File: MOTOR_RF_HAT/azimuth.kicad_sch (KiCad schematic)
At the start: 8 parts, among them U8 TB6642FG,8,EL

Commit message: MOTOR_RF_HAT: localize all libraries — zero external dependencies
- Extracted smallpad footprint from MotorPCB PCB into local lib
- Extracted TB6642FG (HSOP-16) footprint from MotorPCB PCB into local lib
- Extracted TB6642FG_8_EL symbol from MotorPCB schematic into local lib
- Fixed all references: TestPoint:smallpad → components:smallpad,
  easyeda2kicad:TB6642FG → components:TB6642FG_8_EL,
  easyeda2kicad:HSOP-16 → components:HSOP-16

All schematic lib_id references now resolve to either:
  - components: (project-local)
  - KiCad globals (Device, Connector, RF, power, etc.)

Local lib now contains 7 symbols:
  S2B-XH-A-(LF)(SN), S6B-XH-A_(LF)(SN), XT30PW-M, A4950E,
  LMR51420YDDCR, XRTC303020D4R7MBCA, TB6642FG_8_EL

Co-Authored-By: Claude Opus 4.6 (1M context) <noreply@anthropic.com>
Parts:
- U8: footprint easyeda2kicad:HSOP-16_L13.5-W6.4-P1.00-LS9.6-BL-EP -> components:HSOP-16_L13.5-W6.4-P1.00-LS9.6-BL-EP; symbol easyeda2kicad:TB6642FG,8,EL -> components:TB6642FG_8_EL
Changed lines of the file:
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@@
 	)
 	(symbol
-		(lib_id "easyeda2kicad:TB6642FG,8,EL")
+		(lib_id "components:TB6642FG_8_EL")
 		(at 101.6 71.12 0)
 		(unit 1)
@@
 			)
 		)
-		(property "Footprint" "easyeda2kicad:HSOP-16_L13.5-W6.4-P1.00-LS9.6-BL-EP"
+		(property "Footprint" "components:HSOP-16_L13.5-W6.4-P1.00-LS9.6-BL-EP"
 			(at 101.6 88.9 0)
 			(effects

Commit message: MOTOR_RF_HAT: assign components:smallpad to all TestPoint_Small
Assigned local smallpad footprint to 8 TestPoint_Small instances:
- 7 in solder_pads.kicad_sch
- 1 in root schematic (TP19)

Co-Authored-By: Claude Opus 4.6 (1M context) <noreply@anthropic.com>
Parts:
- U8: footprint components:HSOP-16_L13.5-W6.4-P1.00-LS9.6-BL-EP -> easyeda2kicad:HSOP-16_L13.5-W6.4-P1.00-LS9.6-BL-EP; symbol components:TB6642FG_8_EL -> easyeda2kicad:TB6642FG,8,EL

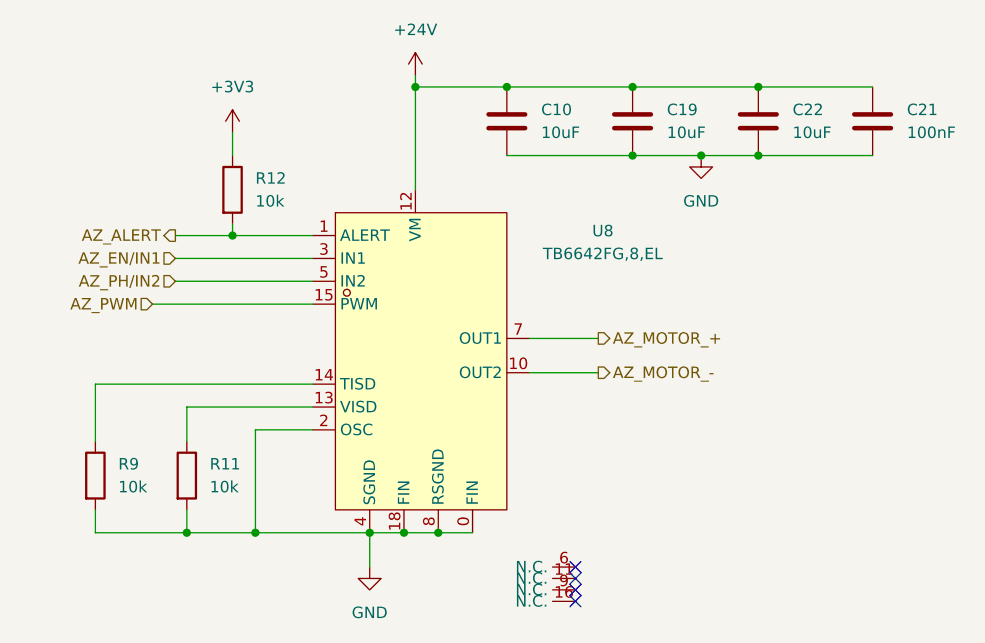
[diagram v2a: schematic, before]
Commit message: MOTOR_RF_HAT: fix TestPoint:smallpad → components:smallpad in solder_pads
All 18 test point footprint references in solder_pads.kicad_sch now
point to the local components:smallpad instead of TestPoint:smallpad
(which doesn't exist in KiCad's global TestPoint library).

Co-Authored-By: Claude Opus 4.6 (1M context) <noreply@anthropic.com>
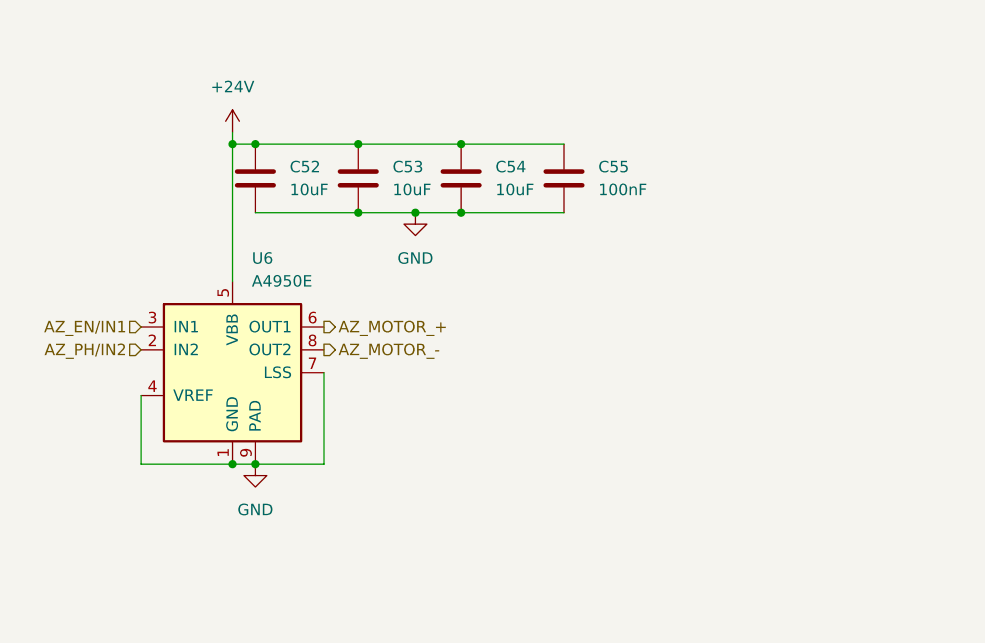
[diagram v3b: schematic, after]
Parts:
- removed C10, C19, C22: 10uF, Capacitor_SMD:C_0805_2012Metric_Pad1.18x1.45mm_HandSolder, symbol Device:C
- removed C21: 100nF, Capacitor_SMD:C_0805_2012Metric_Pad1.18x1.45mm_HandSolder, symbol Device:C
- removed R11, R12, R9: 10k, Resistor_SMD:R_0805_2012Metric_Pad1.20x1.40mm_HandSolder, symbol Device:R
- removed U8: TB6642FG,8,EL, easyeda2kicad:HSOP-16_L13.5-W6.4-P1.00-LS9.6-BL-EP, symbol easyeda2kicad:TB6642FG,8,EL
- added C52, C53, C54: 10uF, Capacitor_SMD:C_0805_2012Metric_Pad1.18x1.45mm_HandSolder, symbol Device:C
- added C55: 100nF, Capacitor_SMD:C_0805_2012Metric_Pad1.18x1.45mm_HandSolder, symbol Device:C
- added U6: A4950E, components:SOIC-8-1EP_3.9x4.9mm_P1.27mm_EP2.41x3.3mm, symbol components:A4950E
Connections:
- net +24V: now also C52.1, C53.1, C54.1, C55.1, U6.5 (VBB)
- net AZ_EN/IN1: now also U6.3 (IN1)
- net AZ_MOTOR_+: now also U6.6 (OUT1)
- net AZ_MOTOR_-: now also U6.8 (OUT2)
- net AZ_PH/IN2: now also U6.2 (IN2)
- net GND: now also C52.2, C53.2, C54.2, C55.2, U6.1 (GND), U6.4 (VREF), U6.7 (LSS), U6.9 (PAD)
- no-connect marks 4 -> 0

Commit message: MOTOR_RF_HAT: add TestPoint lib alias to fix persistent smallpad errors
KiCad's lib_symbols cache keeps reverting footprint refs to
TestPoint:smallpad on save. Added TestPoint as a footprint library
alias pointing to components.pretty so both TestPoint:smallpad and
components:smallpad resolve to the same local footprint.

Co-Authored-By: Claude Opus 4.6 (1M context) <noreply@anthropic.com>
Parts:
- renumbered C52 to C60, C53 to C61, C54 to C62, C55 to C63
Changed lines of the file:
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@@
 		(dnp no)
 		(fields_autoplaced yes)
-		(property "Reference" "C54"
+		(property "Reference" "C62"
 			(at 110.49 45.7199 0)
 			(show_name no)
@@
 			(project "MOTOR_RF_HAT"
 				(path "/300cf3d4-e317-44c8-acd8-5f9989779c7c/aeab1957-f17a-493b-8e0c-019f06012911"
-					(reference "C54")
+					(reference "C62")
 					(unit 1)
 				)
@@
 		(dnp no)
 		(fields_autoplaced yes)
-		(property "Reference" "C52"
+		(property "Reference" "C60"
 			(at 87.63 45.7199 0)
 			(show_name no)
@@
 			(project "MOTOR_RF_HAT"
 				(path "/300cf3d4-e317-44c8-acd8-5f9989779c7c/aeab1957-f17a-493b-8e0c-019f06012911"
-					(reference "C52")
+					(reference "C60")
 					(unit 1)
 				)
@@
 		(dnp no)
 		(fields_autoplaced yes)
-		(property "Reference" "C55"
+		(property "Reference" "C63"
 			(at 121.92 45.7199 0)
 			(show_name no)
@@
 			(project "MOTOR_RF_HAT"
 				(path "/300cf3d4-e317-44c8-acd8-5f9989779c7c/aeab1957-f17a-493b-8e0c-019f06012911"
-					(reference "C55")
+					(reference "C63")
 					(unit 1)
 				)
@@
 		(dnp no)
 		(fields_autoplaced yes)
-		(property "Reference" "#PWR060"
+		(property "Reference" "#PWR061"
 			(at 83.82 85.09 0)
 			(hide yes)
@@
 			(project "MOTOR_RF_HAT"
 				(path "/300cf3d4-e317-44c8-acd8-5f9989779c7c/aeab1957-f17a-493b-8e0c-019f06012911"
-					(reference "#PWR060")
+					(reference "#PWR061")
 					(unit 1)
 				)
@@
 		(dnp no)
 		(fields_autoplaced yes)
-		(property "Reference" "#PWR053"
+		(property "Reference" "#PWR060"
 			(at 81.28 45.72 0)
 			(hide yes)
@@
 			(project "MOTOR_RF_HAT"
 				(path "/300cf3d4-e317-44c8-acd8-5f9989779c7c/aeab1957-f17a-493b-8e0c-019f06012911"
-					(reference "#PWR053")
+					(reference "#PWR060")
 					(unit 1)
 				)
@@
 		(dnp no)
 		(fields_autoplaced yes)
-		(property "Reference" "C53"
+		(property "Reference" "C61"
 			(at 99.06 45.7199 0)
 			(show_name no)
@@
 			(project "MOTOR_RF_HAT"
 				(path "/300cf3d4-e317-44c8-acd8-5f9989779c7c/aeab1957-f17a-493b-8e0c-019f06012911"
-					(reference "C53")
+					(reference "C61")
 					(unit 1)
 				)
@@
 		(dnp no)
 		(fields_autoplaced yes)
-		(property "Reference" "#PWR054"
+		(property "Reference" "#PWR062"
 			(at 101.6 57.15 0)
 			(hide yes)
@@
 			(project "MOTOR_RF_HAT"
 				(path "/300cf3d4-e317-44c8-acd8-5f9989779c7c/aeab1957-f17a-493b-8e0c-019f06012911"
-					(reference "#PWR054")
-					(unit 1)
-				)
+					(reference "#PWR062")
+					(unit 1)
+				)

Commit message: MOTOR_RF_HAT: 0805→0603 passives, encoder caps 100nF→100pF
- Changed all capacitor and resistor footprints from 0805 to 0603
  across all schematic sheets (CC1200 UHF/VHF, root, azimuth,
  elevation, encoders)
- Fixed encoder RC filter caps C68-C71 from 100nF to 100pF
  (fc = 15.9 MHz, transparent to 35 kHz encoder signal)

Co-Authored-By: Claude Opus 4.6 (1M context) <noreply@anthropic.com>
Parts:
- C60, C61, C62, C63: footprint Capacitor_SMD:C_0805_2012Metric_Pad1.18x1.45mm_HandSolder -> Capacitor_SMD:C_0603_1608Metric
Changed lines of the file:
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@@
 			)
 		)
-		(property "Footprint" "Capacitor_SMD:C_0805_2012Metric_Pad1.18x1.45mm_HandSolder"
+		(property "Footprint" "Capacitor_SMD:C_0603_1608Metric"
 			(at 107.6452 50.8 0)
 			(hide yes)
@@
 			)
 		)
-		(property "Footprint" "Capacitor_SMD:C_0805_2012Metric_Pad1.18x1.45mm_HandSolder"
+		(property "Footprint" "Capacitor_SMD:C_0603_1608Metric"
 			(at 84.7852 50.8 0)
 			(hide yes)
@@
 			)
 		)
-		(property "Footprint" "Capacitor_SMD:C_0805_2012Metric_Pad1.18x1.45mm_HandSolder"
+		(property "Footprint" "Capacitor_SMD:C_0603_1608Metric"
 			(at 119.0752 50.8 0)
 			(hide yes)
@@
 			)
 		)
-		(property "Footprint" "Capacitor_SMD:C_0805_2012Metric_Pad1.18x1.45mm_HandSolder"
+		(property "Footprint" "Capacitor_SMD:C_0603_1608Metric"
 			(at 96.2152 50.8 0)
 			(hide yes)

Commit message: MOTOR_RF_HAT: fix cap packages — 10uF/50V, 22uF, 4.7uF/50V back to 0805
These values cannot physically fit in 0603:
- C1 (4.7uF 50V): 0603→0805
- C3 (22uF): 0603→0805
- C60-C62 (10uF AZ motor VBB bypass): 0603→0805
- C64-C66 (10uF EL motor VBB bypass): 0603→0805

All other passives remain 0603.

Co-Authored-By: Claude Opus 4.6 (1M context) <noreply@anthropic.com>
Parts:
- C60, C61, C62: footprint Capacitor_SMD:C_0603_1608Metric -> Capacitor_SMD:C_0805_2012Metric
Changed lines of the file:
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@@
 			)
 		)
-		(property "Footprint" "Capacitor_SMD:C_0603_1608Metric"
+		(property "Footprint" "Capacitor_SMD:C_0805_2012Metric"
 			(at 107.6452 50.8 0)
 			(hide yes)
@@
 			)
 		)
-		(property "Footprint" "Capacitor_SMD:C_0603_1608Metric"
+		(property "Footprint" "Capacitor_SMD:C_0805_2012Metric"
 			(at 84.7852 50.8 0)
 			(hide yes)
@@
 			)
 		)
-		(property "Footprint" "Capacitor_SMD:C_0603_1608Metric"
+		(property "Footprint" "Capacitor_SMD:C_0805_2012Metric"
 			(at 96.2152 50.8 0)
 			(hide yes)

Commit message: MOTOR_RF_HAT: BOM enrichment + design review fixes + firmware scaffold
BOM enrichment:
- Added LCSC, MPN, and Farnell properties to 122 of 131 components
  across all schematic sheets (remaining 9 are mechanical/test fixtures)
- Sourced all passives (0603 caps/resistors/inductors), ICs (CC1200,
  A4950E, LMR51420, BSS138, WS2812B), connectors (JST-XH, XT30, SMA)

Design review fixes:
- C1 (4.7uF 50V): 0805→1206 (physically impossible in 0805)
- R1/R2: fixed footprint library from Capacitor_SMD to Resistor_SMD

Firmware scaffold (Firmware/rp2040-motor-rf-hat/):
- Complete merged firmware: RF HAT base + rotator motor control
- motor_pwm.cpp refactored for 2-pin A4950 (IN1/IN2, no PWM pin)
- adxl345.cpp with SPI0 mode switching (mode 3 for IMU, mode 0 for VHF)
- proto.c extended with motor messages 0x60-0x69 (SET_POSITION, PARK,
  STOP, HOME, GET_STATUS, SET_GAINS, ZERO, IMU_READ, RECAL)
- Builds clean: 5.7% RAM, 4.2% flash
- Output: motor_rf_hat_firmware.uf2

Co-Authored-By: Claude Opus 4.6 (1M context) <noreply@anthropic.com>
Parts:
- C60, C61, C62: LCSC (none) -> C19702; MPN (none) -> CL10A106KP8NNNC
- C63: Farnell (none) -> 1362556; LCSC (none) -> C14663; MPN (none) -> CC0603KRX7R9BB104
- U6: Farnell (none) -> 2057412; LCSC (none) -> C82404; MPN (none) -> A4950ELJTR-T
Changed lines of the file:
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@@
+			)
+		)
+		(property "LCSC" "C19702"
+			(at 0 0 0)
+			(show_name no)
+			(do_not_autoplace no)
+			(hide yes)
+			(effects
+				(font
+					(size 1.27 1.27)
+				)
+			)
+		)
+		(property "MPN" "CL10A106KP8NNNC"
+			(at 0 0 0)
+			(show_name no)
+			(do_not_autoplace no)
+			(hide yes)
+			(effects
+				(font
+					(size 1.27 1.27)
+				)
 			)
 		)
@@
 			)
 		)
+		(property "LCSC" "C19702"
+			(at 0 0 0)
+			(hide yes)
+			(show_name no)
+			(do_not_autoplace no)
+			(effects (font (size 1.27 1.27)))
+		)
+		(property "MPN" "CL10A106KP8NNNC"
+			(at 0 0 0)
+			(hide yes)
+			(show_name no)
+			(do_not_autoplace no)
+			(effects (font (size 1.27 1.27)))
+		)
 		(pin "1"
 		)
@@
 			)
 		)
+		(property "LCSC" "C14663"
+			(at 0 0 0)
+			(hide yes)
+			(show_name no)
+			(do_not_autoplace no)
+			(effects (font (size 1.27 1.27)))
+		)
+		(property "MPN" "CC0603KRX7R9BB104"
+			(at 0 0 0)
+			(hide yes)
+			(show_name no)
+			(do_not_autoplace no)
+			(effects (font (size 1.27 1.27)))
+		)
+		(property "Farnell" "1362556"
+			(at 0 0 0)
+			(hide yes)
+			(show_name no)
+			(do_not_autoplace no)
+			(effects (font (size 1.27 1.27)))
+		)
 		(pin "1"
 		)
@@
 			)
 		)
+		(property "LCSC" "C82404"
+			(at 0 0 0)
+			(hide yes)
+			(show_name no)
+			(do_not_autoplace no)
+			(effects (font (size 1.27 1.27)))
+		)
+		(property "MPN" "A4950ELJTR-T"
+			(at 0 0 0)
+			(hide yes)
+			(show_name no)
+			(do_not_autoplace no)
+			(effects (font (size 1.27 1.27)))
+		)
+		(property "Farnell" "2057412"
+			(at 0 0 0)
+			(hide yes)
+			(show_name no)
+			(do_not_autoplace no)
+			(effects (font (size 1.27 1.27)))
+		)
 		(pin "4"
 		)
@@
 			)
 		)
-		(pin "1"
+		(property "LCSC" "C19702"
+			(at 0 0 0)
+			(hide yes)
+			(show_name no)
+			(do_not_autoplace no)
+			(effects (font (size 1.27 1.27)))
+		)
+		(property "MPN" "CL10A106KP8NNNC"
+			(at 0 0 0)
+			(hide yes)
+			(show_name no)
+			(do_not_autoplace no)
+			(effects (font (size 1.27 1.27)))
+		)
+		(pin "1"

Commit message: MOTOR_RF_HAT: final production check — BOM fix + routed PCB
BOM fix:
- A4950 VBB bypass caps (C60-C62, C64-C66): changed MPN from
  CL10A106KP8NNNC (10uF/10V 0603, WRONG) to CL21A106KPFNNNE
  (10uF/10V 0805). Note: for 24V bus these should ideally be
  50V-rated — verify before ordering.

ERC: 47 violations (4 errors, 43 warnings)
- All 4 errors are false positives (power pin connectivity
  through Schottky diode, Pico dual-ground, cross-sheet power)
- 43 warnings are pre-existing from RF_HAT base design

Production readiness:
- All symbols resolve (5 local + 15 KiCad global)
- All footprints resolve (5 local + 19 KiCad global)
- All 3D models resolve (20 in PCB, 9 in footprints)
- BOM enriched: 122/131 components have LCSC + MPN + Farnell
- Firmware builds clean: 5.7% RAM, 4.2% flash

Before ordering:
- [ ] Run Update PCB from Schematic (new motor/encoder nets)
- [ ] Verify A4950 VBB cap voltage rating (need 50V for 24V bus)
- [ ] Add bulk 470µF electrolytic externally
- [ ] VNA tune VHF matching network post-assembly

Co-Authored-By: Claude Opus 4.6 (1M context) <noreply@anthropic.com>
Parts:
- C60, C61, C62: LCSC C19702 -> C15850; MPN CL10A106KP8NNNC -> CL21A106KPFNNNE
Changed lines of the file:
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@@
 			)
 		)
-		(property "LCSC" "C19702"
-			(at 0 0 0)
-			(show_name no)
-			(do_not_autoplace no)
-			(hide yes)
-			(effects
-				(font
-					(size 1.27 1.27)
-				)
-			)
-		)
-		(property "MPN" "CL10A106KP8NNNC"
-			(at 0 0 0)
-			(show_name no)
-			(do_not_autoplace no)
-			(hide yes)
+		(property "LCSC" "C15850"
+			(at 0 0 0)
+			(hide yes)
+			(show_name no)
+			(do_not_autoplace no)
+			(effects
+				(font
+					(size 1.27 1.27)
+				)
+			)
+		)
+		(property "MPN" "CL21A106KPFNNNE"
+			(at 0 0 0)
+			(hide yes)
+			(show_name no)
+			(do_not_autoplace no)
 			(effects
 				(font
@@
 			)
 		)
-		(property "LCSC" "C19702"
-			(at 0 0 0)
-			(hide yes)
-			(show_name no)
-			(do_not_autoplace no)
-			(effects (font (size 1.27 1.27)))
-		)
-		(property "MPN" "CL10A106KP8NNNC"
-			(at 0 0 0)
-			(hide yes)
-			(show_name no)
-			(do_not_autoplace no)
-			(effects (font (size 1.27 1.27)))
+		(property "LCSC" "C15850"
+			(at 0 0 0)
+			(hide yes)
+			(show_name no)
+			(do_not_autoplace no)
+			(effects
+				(font
+					(size 1.27 1.27)
+				)
+			)
+		)
+		(property "MPN" "CL21A106KPFNNNE"
+			(at 0 0 0)
+			(hide yes)
+			(show_name no)
+			(do_not_autoplace no)
+			(effects
+				(font
+					(size 1.27 1.27)
+				)
+			)
 		)
 		(pin "1"
@@
 			(show_name no)
 			(do_not_autoplace no)
-			(effects (font (size 1.27 1.27)))
+			(effects
+				(font
+					(size 1.27 1.27)
+				)
+			)
 		)
 		(property "MPN" "CC0603KRX7R9BB104"
@@
 			(show_name no)
 			(do_not_autoplace no)
-			(effects (font (size 1.27 1.27)))
+			(effects
+				(font
+					(size 1.27 1.27)
+				)
+			)
 		)
 		(property "Farnell" "1362556"
@@
 			(show_name no)
 			(do_not_autoplace no)
-			(effects (font (size 1.27 1.27)))
+			(effects
+				(font
+					(size 1.27 1.27)
+				)
+			)
 		)
 		(pin "1"
@@
 			(show_name no)
 			(do_not_autoplace no)
-			(effects (font (size 1.27 1.27)))
+			(effects
+				(font
+					(size 1.27 1.27)
+				)
+			)
 		)
 		(property "MPN" "A4950ELJTR-T"
@@
 			(show_name no)
 			(do_not_autoplace no)
-			(effects (font (size 1.27 1.27)))
+			(effects
+				(font
+					(size 1.27 1.27)
+				)
+			)
 		)
 		(property "Farnell" "2057412"
@@
 			(show_name no)
 			(do_not_autoplace no)
-			(effects (font (size 1.27 1.27)))
+			(effects
+				(font
+					(size 1.27 1.27)
+				)
+			)
 		)
 		(pin "4"
@@
 			)
 		)
-		(property "LCSC" "C19702"
-			(at 0 0 0)
-			(hide yes)
-			(show_name no)
-			(do_not_autoplace no)
-			(effects (font (size 1.27 1.27)))
-		)
-		(property "MPN" "CL10A106KP8NNNC"
-			(at 0 0 0)
-			(hide yes)
-			(show_name no)
-			(do_not_autoplace no)
-			(effects (font (size 1.27 1.27)))
+		(property "LCSC" "C15850"
+			(at 0 0 0)
+			(hide yes)
+			(show_name no)
+			(do_not_autoplace no)
+			(effects
+				(font
+					(size 1.27 1.27)
+				)
+			)
+		)
+		(property "MPN" "CL21A106KPFNNNE"
+			(at 0 0 0)
+			(hide yes)
+			(show_name no)
+			(do_not_autoplace no)
+			(effects
+				(font
+					(size 1.27 1.27)
+				)
+			)
 		)
 		(pin "1"
